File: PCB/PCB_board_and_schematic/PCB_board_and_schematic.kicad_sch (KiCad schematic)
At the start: 0 parts

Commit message: Added the needed components to the schematic design.
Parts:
- added C1: 100nF, symbol Device:C
- added C2: 10µF, symbol Device:C
- added D1, D2: BAT54S, Package_TO_SOT_SMD:SOT-23, symbol Diode:BAT54S
- added J1: TangoNano9k_topSide, symbol Connector:Conn_01x24_Socket
- added J2: TangoNano9k_bottomSide, symbol Connector:Conn_01x24_Socket
- added J3: TheSensor, symbol Connector:Conn_01x04_Socket
- added Q1, Q2: Q_PMOS_GDS, symbol Transistor_FET:Q_PMOS_GDS
- added R1, R2: 4.7KΩ, symbol Device:R
- added R3, R4: 220Ω, symbol Device:R
- added R5, R6: 10KΩ, symbol Device:R
- added R7, R8: 100Ω, symbol Device:R
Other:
- company: (none) -> MHD YASIN AL ARJAWI
- title: (none) -> Tang Nano 9k Bus identifier

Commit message: Changed some components in the schematic design (added diodes and deleted BAT54S)
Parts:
- removed D1, D2: BAT54S, Package_TO_SOT_SMD:SOT-23, symbol Diode:BAT54S
- added D1, D2, D3, D4: D, symbol Device:D

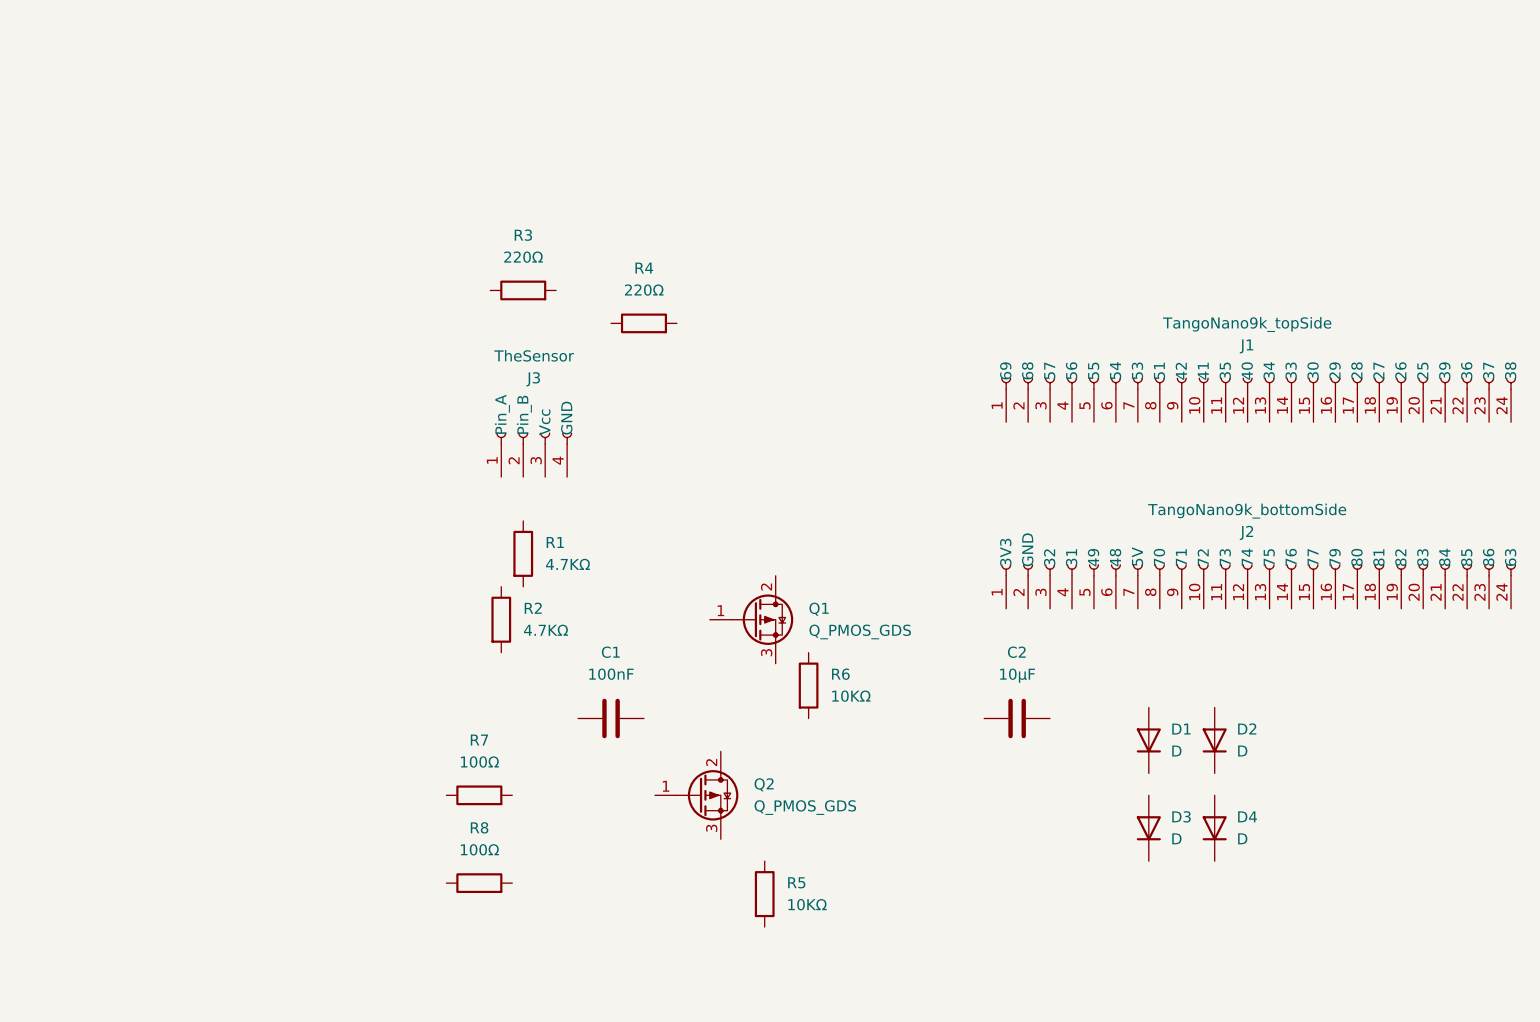
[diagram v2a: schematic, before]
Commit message: wired schematic design (except FPGA pins, not selected for now).
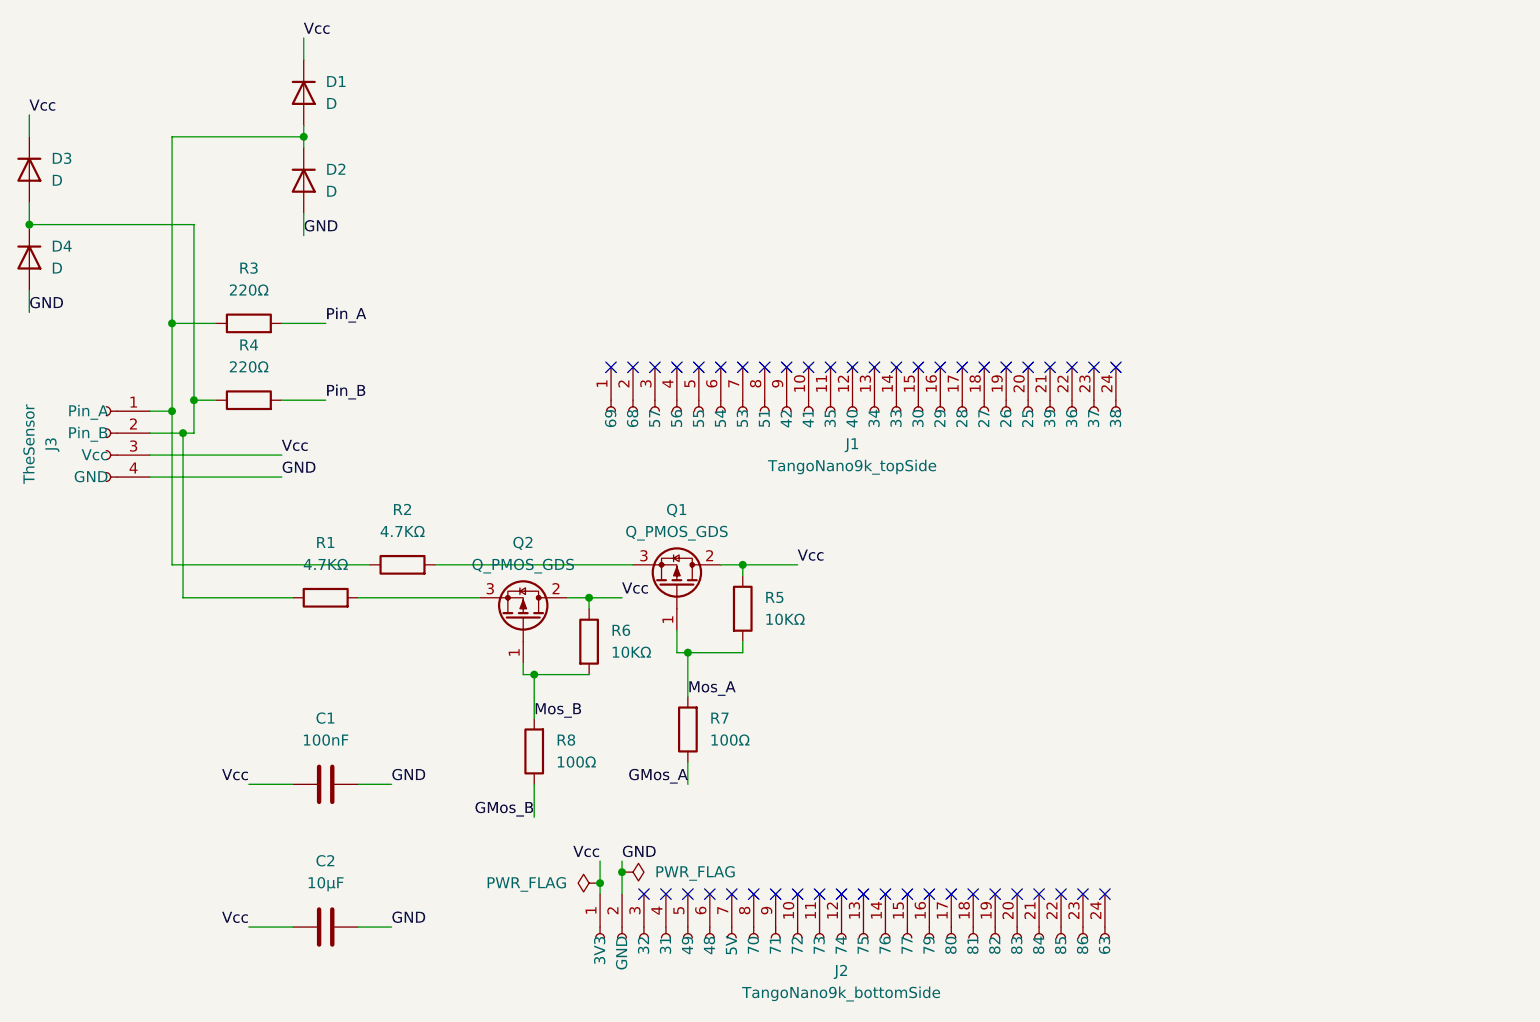
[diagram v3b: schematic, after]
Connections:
- net Vcc: now reaches D3.1 (K)
- net Vcc: now also C1.1, C2.1, D1.1 (K), J2.1 (3V3), J3.3 (Vcc), Q1.2 (D), Q2.2 (D), R5.1, R6.1
- net at D3.2 (A): now also D4.1 (K), J3.2 (Pin_B), R1.1, R4.1
- net GMos_B: now reaches R8.1
- net Mos_B: now reaches R8.2
- net Mos_B: now also Q2.1 (G), R6.2
- net at Q2.3 (S): now also R1.2
- net GND: now reaches C2.2
- net GND: now also C1.2, D2.2 (A), D4.2 (A), J2.2 (GND), J3.4 (GND)
- net at R3.1: now also D1.2 (A), D2.1 (K), J3.1 (Pin_A), R2.1
- net Pin_A: now reaches R3.2
- net Pin_B: now reaches R4.2
- net at R2.2: now also Q1.3 (S)
- net Mos_A: now reaches Q1.1 (G)
- net Mos_A: now also R5.2, R7.2
- net GMos_A: now reaches R7.1
- no-connect marks 0 -> 46
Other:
- moved on the sheet: C1, C2, D1, D2, D3, D4, J1, J2, J3, Q1, Q2, R1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

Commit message: Fixed PCB schematic (mosfet placement) and finished the full PCB design (except the Pin_a, Pin_b, and the mosfets gates because not selected yet)
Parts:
- C1: footprint (none) -> Capacitor_THT:CP_Radial_D4.0mm_P1.50mm
- C2: footprint (none) -> Capacitor_THT:CP_Radial_D5.0mm_P2.50mm
- D1, D2, D3, D4: footprint (none) -> Diode_THT:D_A-405_P7.62mm_Horizontal
- J1, J2: footprint (none) -> Connector_PinSocket_2.54mm:PinSocket_1x24_P2.54mm_Vertical
- J3: footprint (none) -> Connector_PinSocket_2.54mm:PinSocket_1x04_P2.54mm_Vertical
- Q1, Q2: footprint (none) -> Package_TO_SOT_THT:TO-220-3_Vertical
- R1, R2, R3, R4, R5, R6, R7, R8: footprint (none) -> Resistor_THT:R_Axial_DIN0204_L3.6mm_D1.6mm_P7.62mm_Horizontal
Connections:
- net Vcc: now also Q1.3 (S), Q2.3 (S); no longer Q1.2 (D), Q2.2 (D)
- net at R1.2: now also Q2.2 (D); no longer Q2.3 (S)
- net at R2.2: now also Q1.2 (D); no longer Q1.3 (S)
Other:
- moved on the sheet: Q1, Q2
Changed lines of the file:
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@@
 			)
 		)
-		(property "Footprint" ""
+		(property "Footprint" "Diode_THT:D_A-405_P7.62mm_Horizontal"
 			(at 77.47 43.18 0)
 			(hide yes)
@@
 			)
 		)
-		(property "Footprint" ""
+		(property "Footprint" "Resistor_THT:R_Axial_DIN0204_L3.6mm_D1.6mm_P7.62mm_Horizontal"
 			(at 137.668 110.49 90)
 			(hide yes)
@@
 	(symbol
 		(lib_id "Transistor_FET:Q_PMOS_GDS")
-		(at 134.62 95.25 270)
-		(mirror x)
+		(at 134.62 95.25 90)
 		(unit 1)
 		(body_style 1)
@@
 			)
 		)
-		(property "Footprint" ""
-			(at 137.16 90.17 0)
+		(property "Footprint" "Package_TO_SOT_THT:TO-220-3_Vertical"
+			(at 132.08 90.17 0)
 			(hide yes)
 			(show_name no)
@@
 			)
 		)
-		(property "Footprint" ""
+		(property "Footprint" "Capacitor_THT:CP_Radial_D5.0mm_P2.50mm"
 			(at 115.57 129.8448 0)
 			(hide yes)
@@
 			)
 		)
-		(property "Footprint" ""
+		(property "Footprint" "Resistor_THT:R_Axial_DIN0204_L3.6mm_D1.6mm_P7.62mm_Horizontal"
 			(at 102.87 62.738 90)
 			(hide yes)
@@
 			)
 		)
-		(property "Footprint" ""
+		(property "Footprint" "Connector_PinSocket_2.54mm:PinSocket_1x24_P2.54mm_Vertical"
 			(at 172.72 71.12 0)
 			(hide yes)
@@
 			)
 		)
-		(property "Footprint" ""
+		(property "Footprint" "Capacitor_THT:CP_Radial_D4.0mm_P1.50mm"
 			(at 115.57 115.2652 0)
 			(hide yes)
@@
 			)
 		)
-		(property "Footprint" ""
+		(property "Footprint" "Connector_PinSocket_2.54mm:PinSocket_1x24_P2.54mm_Vertical"
 			(at 171.45 132.08 0)
 			(hide yes)
@@
 			)
 		)
-		(property "Footprint" ""
+		(property "Footprint" "Diode_THT:D_A-405_P7.62mm_Horizontal"
 			(at 77.47 53.34 0)
 			(hide yes)
@@
 			)
 		)
-		(property "Footprint" ""
+		(property "Footprint" "Resistor_THT:R_Axial_DIN0204_L3.6mm_D1.6mm_P7.62mm_Horizontal"
 			(at 140.462 97.79 90)
 			(hide yes)
@@
 			)
 		)
-		(property "Footprint" ""
+		(property "Footprint" "Diode_THT:D_A-405_P7.62mm_Horizontal"
 			(at 109.22 34.29 0)
 			(hide yes)
@@
 			)
 		)
-		(property "Footprint" ""
+		(property "Footprint" "Resistor_THT:R_Axial_DIN0204_L3.6mm_D1.6mm_P7.62mm_Horizontal"
 			(at 111.76 94.488 90)
 			(hide yes)
@@
 			)
 		)
-		(property "Footprint" ""
+		(property "Footprint" "Resistor_THT:R_Axial_DIN0204_L3.6mm_D1.6mm_P7.62mm_Horizontal"
 			(at 102.87 71.628 90)
 			(hide yes)
@@
 			)
 		)
-		(property "Footprint" ""
+		(property "Footprint" "Connector_PinSocket_2.54mm:PinSocket_1x04_P2.54mm_Vertical"
 			(at 86.36 73.66 0)
 			(hide yes)
@@
 			)
 		)
-		(property "Footprint" ""
+		(property "Footprint" "Diode_THT:D_A-405_P7.62mm_Horizontal"
 			(at 109.22 44.45 0)
 			(hide yes)
@@
 			)
 		)
-		(property "Footprint" ""
+		(property "Footprint" "Resistor_THT:R_Axial_DIN0204_L3.6mm_D1.6mm_P7.62mm_Horizontal"
 			(at 120.65 90.678 90)
 			(hide yes)
@@
 	(symbol
 		(lib_id "Transistor_FET:Q_PMOS_GDS")
-		(at 152.4 91.44 270)
-		(mirror x)
+		(at 152.4 91.44 90)
 		(unit 1)
 		(body_style 1)
@@
 			)
 		)
-		(property "Footprint" ""
-			(at 154.94 86.36 0)
+		(property "Footprint" "Package_TO_SOT_THT:TO-220-3_Vertical"
+			(at 149.86 86.36 0)
 			(hide yes)
 			(show_name no)
@@
 			)
 		)
-		(property "Footprint" ""
+		(property "Footprint" "Resistor_THT:R_Axial_DIN0204_L3.6mm_D1.6mm_P7.62mm_Horizontal"
 			(at 158.242 93.98 90)
 			(hide yes)
@@
 			)
 		)
-		(property "Footprint" ""
+		(property "Footprint" "Resistor_THT:R_Axial_DIN0204_L3.6mm_D1.6mm_P7.62mm_Horizontal"
 			(at 155.448 107.95 90)
 			(hide yes)

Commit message: finished PCB design completly.
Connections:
- net GMos_A: now also J1.5 (55)
- net GMos_B: now also J1.6 (54)
- net Pin_A: now also J1.4 (56)
- net Pin_B: now also J1.3 (57)
- no-connect marks 46 -> 42
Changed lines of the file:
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@@
-	)
-	(no_connect
-		(at 154.94 66.04)
 	)
 	(no_connect
@@
 	)
 	(no_connect
-		(at 157.48 66.04)
-	)
-	(no_connect
-		(at 152.4 66.04)
-	)
-	(no_connect
 		(at 195.58 66.04)
 	)
@@
 	)
 	(no_connect
-		(at 149.86 66.04)
-	)
-	(no_connect
 		(at 194.31 127)
 	)
@@
 	(wire
 		(pts
+			(xy 152.4 58.42) (xy 152.4 66.04)
+		)
+		(stroke
+			(width 0)
+			(type default)
+		)
+	)
+	(wire
+		(pts
+			(xy 157.48 63.5) (xy 157.48 66.04)
+		)
+		(stroke
+			(width 0)
+			(type default)
+		)
+	)
+	(wire
+		(pts
 			(xy 96.52 49.53) (xy 77.47 49.53)
 		)
@@
 	(wire
 		(pts
+			(xy 154.94 60.96) (xy 154.94 66.04)
+		)
+		(stroke
+			(width 0)
+			(type default)
+		)
+	)
+	(wire
+		(pts
 			(xy 160.02 99.06) (xy 160.02 97.79)
 		)
@@
 		(pts
 			(xy 119.38 130.81) (xy 115.57 130.81)
+		)
+		(stroke
+			(width 0)
+			(type default)
+		)
+	)
+	(wire
+		(pts
+			(xy 149.86 58.42) (xy 149.86 66.04)
 		)
 		(stroke
@@
 		)
 	)
+	(label "GMos_B"
+		(at 157.48 63.5 0)
+		(effects
+			(font
+				(size 1.27 1.27)
+			)
+			(justify left bottom)
+		)
+	)
 	(label "Pin_B"
 		(at 111.76 69.85 0)
@@
 		)
 	)
+	(label "GMos_A"
+		(at 154.94 60.96 0)
+		(effects
+			(font
+				(size 1.27 1.27)
+			)
+			(justify left bottom)
+		)
+	)
+	(label "Pin_B"
+		(at 149.86 58.42 180)
+		(effects
+			(font
+				(size 1.27 1.27)
+			)
+			(justify right bottom)
+		)
+	)
 	(label "Vcc"
 		(at 109.22 27.94 0)
@@
 		(effects
 			(font
+				(size 1.27 1.27)
+			)
+			(justify left bottom)
+		)
+	)
+	(label "Pin_A"
+		(at 152.4 58.42 0)
+		(effects
+			(font
